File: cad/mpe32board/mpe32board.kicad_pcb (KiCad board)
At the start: 2 copper layers, 2 parts, among them J1 Conn_ST_STDC14, U2 STM32H743VIHx

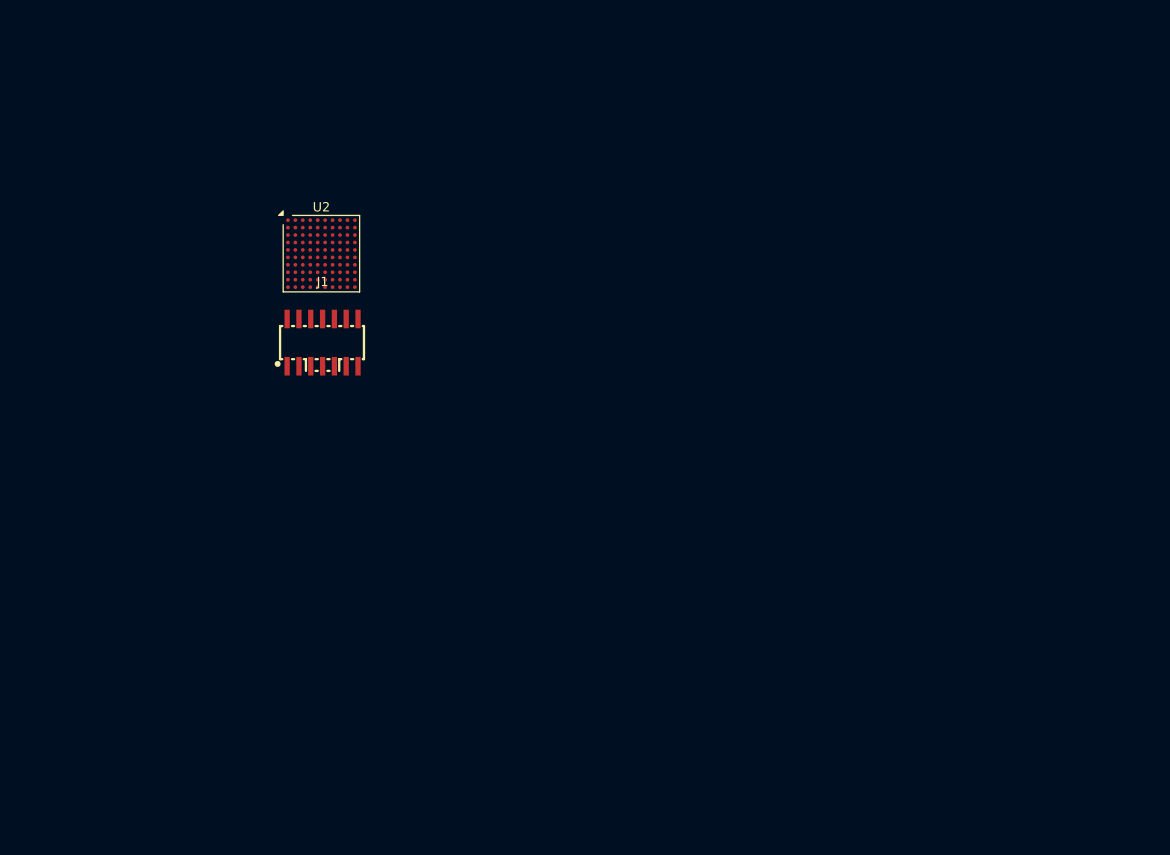
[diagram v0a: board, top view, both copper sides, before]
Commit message: pcb i2c mux + connectors
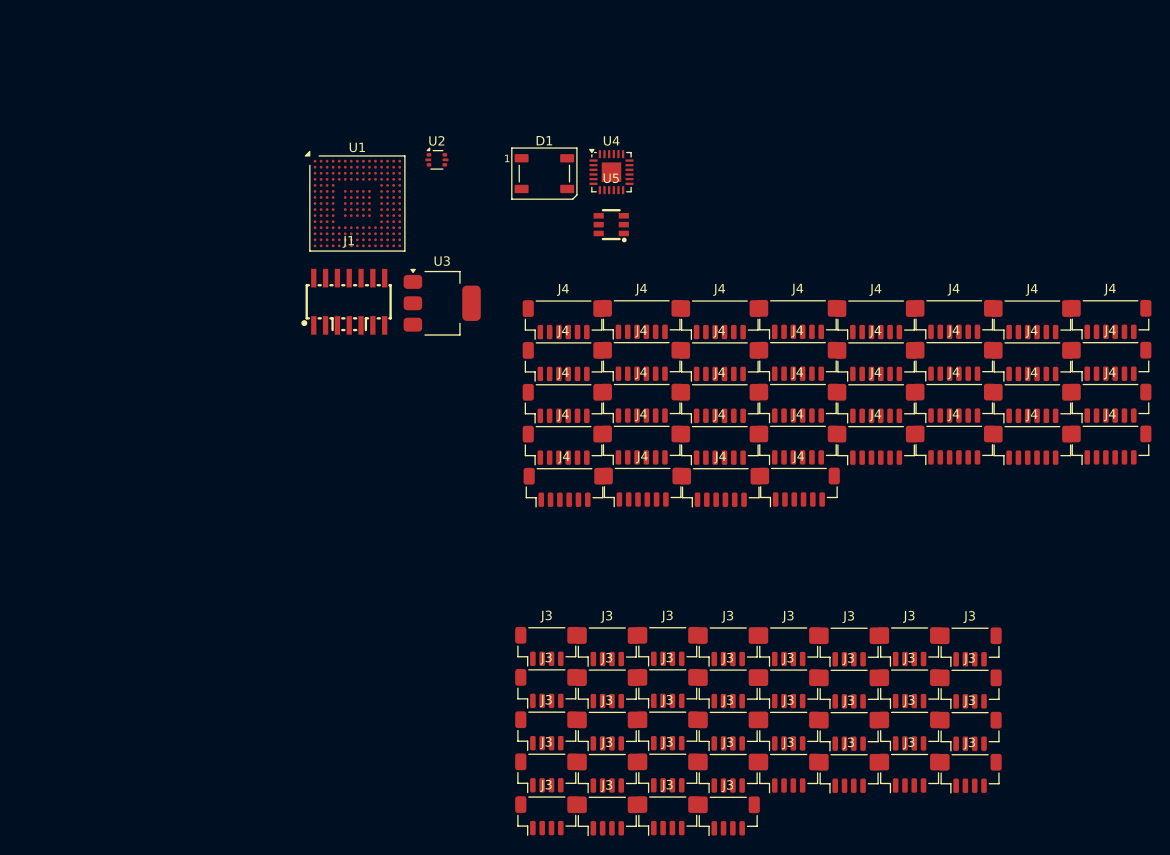
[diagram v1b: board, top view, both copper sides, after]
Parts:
- added D1: WS2812B, LED_SMD:LED_WS2812B_PLCC4_5.0x5.0mm_P3.2mm, F.Cu at (155.0, 84.3)
- added J3: Conn_01x04, Connector_JST:JST_SH_BM04B-SRSS-TB_1x04-1MP_P1.00mm_Vertical, F.Cu at (174.8, 153.3)
- added J3: Conn_01x04, Connector_JST:JST_SH_BM04B-SRSS-TB_1x04-1MP_P1.00mm_Vertical, F.Cu at (194.3, 139.7)
- added J3: Conn_01x04, Connector_JST:JST_SH_BM04B-SRSS-TB_1x04-1MP_P1.00mm_Vertical, F.Cu at (200.8, 139.7)
- added J3: Conn_01x04, Connector_JST:JST_SH_BM04B-SRSS-TB_1x04-1MP_P1.00mm_Vertical, F.Cu at (194.3, 144.2)
- added J3: Conn_01x04, Connector_JST:JST_SH_BM04B-SRSS-TB_1x04-1MP_P1.00mm_Vertical, F.Cu at (161.8, 139.7)
- added J3: Conn_01x04, Connector_JST:JST_SH_BM04B-SRSS-TB_1x04-1MP_P1.00mm_Vertical, F.Cu at (168.3, 144.2)
- added J3: Conn_01x04, Connector_JST:JST_SH_BM04B-SRSS-TB_1x04-1MP_P1.00mm_Vertical, F.Cu at (155.3, 135.1)
- added J3: Conn_01x04, Connector_JST:JST_SH_BM04B-SRSS-TB_1x04-1MP_P1.00mm_Vertical, F.Cu at (187.8, 148.8)
- added J3: Conn_01x04, Connector_JST:JST_SH_BM04B-SRSS-TB_1x04-1MP_P1.00mm_Vertical, F.Cu at (161.8, 148.8)
- added J3: Conn_01x04, Connector_JST:JST_SH_BM04B-SRSS-TB_1x04-1MP_P1.00mm_Vertical, F.Cu at (200.8, 135.2)
- added J3: Conn_01x04, Connector_JST:JST_SH_BM04B-SRSS-TB_1x04-1MP_P1.00mm_Vertical, F.Cu at (187.8, 144.2)
- added J3: Conn_01x04, Connector_JST:JST_SH_BM04B-SRSS-TB_1x04-1MP_P1.00mm_Vertical, F.Cu at (181.3, 139.7)
- added J3: Conn_01x04, Connector_JST:JST_SH_BM04B-SRSS-TB_1x04-1MP_P1.00mm_Vertical, F.Cu at (168.3, 148.7)
- added J3: Conn_01x04, Connector_JST:JST_SH_BM04B-SRSS-TB_1x04-1MP_P1.00mm_Vertical, F.Cu at (200.8, 148.8)
- added J3: Conn_01x04, Connector_JST:JST_SH_BM04B-SRSS-TB_1x04-1MP_P1.00mm_Vertical, F.Cu at (181.3, 148.8)
- added J3: Conn_01x04, Connector_JST:JST_SH_BM04B-SRSS-TB_1x04-1MP_P1.00mm_Vertical, F.Cu at (174.8, 144.2)
- added J3: Conn_01x04, Connector_JST:JST_SH_BM04B-SRSS-TB_1x04-1MP_P1.00mm_Vertical, F.Cu at (168.3, 139.7)
- added J3: Conn_01x04, Connector_JST:JST_SH_BM04B-SRSS-TB_1x04-1MP_P1.00mm_Vertical, F.Cu at (155.3, 139.7)
- added J3: Conn_01x04, Connector_JST:JST_SH_BM04B-SRSS-TB_1x04-1MP_P1.00mm_Vertical, F.Cu at (161.8, 144.2)
- added J3: Conn_01x04, Connector_JST:JST_SH_BM04B-SRSS-TB_1x04-1MP_P1.00mm_Vertical, F.Cu at (174.8, 135.2)
- added J3: Conn_01x04, Connector_JST:JST_SH_BM04B-SRSS-TB_1x04-1MP_P1.00mm_Vertical, F.Cu at (187.8, 135.2)
- added J3: Conn_01x04, Connector_JST:JST_SH_BM04B-SRSS-TB_1x04-1MP_P1.00mm_Vertical, F.Cu at (187.8, 139.7)
- added J3: Conn_01x04, Connector_JST:JST_SH_BM04B-SRSS-TB_1x04-1MP_P1.00mm_Vertical, F.Cu at (194.3, 148.8)
- added J3: Conn_01x04, Connector_JST:JST_SH_BM04B-SRSS-TB_1x04-1MP_P1.00mm_Vertical, F.Cu at (200.8, 144.2)
- added J3: Conn_01x04, Connector_JST:JST_SH_BM04B-SRSS-TB_1x04-1MP_P1.00mm_Vertical, F.Cu at (174.8, 148.8)
- added J3: Conn_01x04, Connector_JST:JST_SH_BM04B-SRSS-TB_1x04-1MP_P1.00mm_Vertical, F.Cu at (155.3, 153.3)
- added J3: Conn_01x04, Connector_JST:JST_SH_BM04B-SRSS-TB_1x04-1MP_P1.00mm_Vertical, F.Cu at (194.3, 135.2)
- added J3: Conn_01x04, Connector_JST:JST_SH_BM04B-SRSS-TB_1x04-1MP_P1.00mm_Vertical, F.Cu at (155.3, 144.2)
- added J3: Conn_01x04, Connector_JST:JST_SH_BM04B-SRSS-TB_1x04-1MP_P1.00mm_Vertical, F.Cu at (181.3, 144.2)
- added J3: Conn_01x04, Connector_JST:JST_SH_BM04B-SRSS-TB_1x04-1MP_P1.00mm_Vertical, F.Cu at (181.3, 135.2)
- added J3: Conn_01x04, Connector_JST:JST_SH_BM04B-SRSS-TB_1x04-1MP_P1.00mm_Vertical, F.Cu at (168.3, 135.1)
- added J3: Conn_01x04, Connector_JST:JST_SH_BM04B-SRSS-TB_1x04-1MP_P1.00mm_Vertical, F.Cu at (161.8, 135.2)
- added J3: Conn_01x04, Connector_JST:JST_SH_BM04B-SRSS-TB_1x04-1MP_P1.00mm_Vertical, F.Cu at (174.8, 139.7)
- added J3: Conn_01x04, Connector_JST:JST_SH_BM04B-SRSS-TB_1x04-1MP_P1.00mm_Vertical, F.Cu at (168.3, 153.3)
- added J3: Conn_01x04, Connector_JST:JST_SH_BM04B-SRSS-TB_1x04-1MP_P1.00mm_Vertical, F.Cu at (161.8, 153.3)
- added J3: Conn_01x04, Connector_JST:JST_SH_BM04B-SRSS-TB_1x04-1MP_P1.00mm_Vertical, F.Cu at (155.3, 148.7)
- added J4: Conn_01x06, Connector_JST:JST_SH_BM06B-SRSS-TB_1x06-1MP_P1.00mm_Vertical, F.Cu at (215.9, 100.0)
- added J4: Conn_01x06, Connector_JST:JST_SH_BM06B-SRSS-TB_1x06-1MP_P1.00mm_Vertical, F.Cu at (165.5, 104.5)
- added J4: Conn_01x06, Connector_JST:JST_SH_BM06B-SRSS-TB_1x06-1MP_P1.00mm_Vertical, F.Cu at (190.7, 100.0)
- added J4: Conn_01x06, Connector_JST:JST_SH_BM06B-SRSS-TB_1x06-1MP_P1.00mm_Vertical, F.Cu at (182.4, 118.0)
- added J4: Conn_01x06, Connector_JST:JST_SH_BM06B-SRSS-TB_1x06-1MP_P1.00mm_Vertical, F.Cu at (190.7, 109.0)
- added J4: Conn_01x06, Connector_JST:JST_SH_BM06B-SRSS-TB_1x06-1MP_P1.00mm_Vertical, F.Cu at (199.1, 109.0)
- added J4: Conn_01x06, Connector_JST:JST_SH_BM06B-SRSS-TB_1x06-1MP_P1.00mm_Vertical, F.Cu at (157.1, 100.0)
- added J4: Conn_01x06, Connector_JST:JST_SH_BM06B-SRSS-TB_1x06-1MP_P1.00mm_Vertical, F.Cu at (182.3, 104.5)
- added J4: Conn_01x06, Connector_JST:JST_SH_BM06B-SRSS-TB_1x06-1MP_P1.00mm_Vertical, F.Cu at (207.5, 109.0)
- added J4: Conn_01x06, Connector_JST:JST_SH_BM06B-SRSS-TB_1x06-1MP_P1.00mm_Vertical, F.Cu at (207.5, 113.5)
- added J4: Conn_01x06, Connector_JST:JST_SH_BM06B-SRSS-TB_1x06-1MP_P1.00mm_Vertical, F.Cu at (165.5, 109.0)
- added J4: Conn_01x06, Connector_JST:JST_SH_BM06B-SRSS-TB_1x06-1MP_P1.00mm_Vertical, F.Cu at (215.9, 104.5)
- added J4: Conn_01x06, Connector_JST:JST_SH_BM06B-SRSS-TB_1x06-1MP_P1.00mm_Vertical, F.Cu at (173.9, 113.5)
- added J4: Conn_01x06, Connector_JST:JST_SH_BM06B-SRSS-TB_1x06-1MP_P1.00mm_Vertical, F.Cu at (215.9, 113.5)
- added J4: Conn_01x06, Connector_JST:JST_SH_BM06B-SRSS-TB_1x06-1MP_P1.00mm_Vertical, F.Cu at (173.9, 104.5)
- added J4: Conn_01x06, Connector_JST:JST_SH_BM06B-SRSS-TB_1x06-1MP_P1.00mm_Vertical, F.Cu at (157.1, 104.5)
- added J4: Conn_01x06, Connector_JST:JST_SH_BM06B-SRSS-TB_1x06-1MP_P1.00mm_Vertical, F.Cu at (207.5, 100.0)
- added J4: Conn_01x06, Connector_JST:JST_SH_BM06B-SRSS-TB_1x06-1MP_P1.00mm_Vertical, F.Cu at (157.1, 113.5)
- added J4: Conn_01x06, Connector_JST:JST_SH_BM06B-SRSS-TB_1x06-1MP_P1.00mm_Vertical, F.Cu at (182.3, 109.0)
- added J4: Conn_01x06, Connector_JST:JST_SH_BM06B-SRSS-TB_1x06-1MP_P1.00mm_Vertical, F.Cu at (165.5, 113.5)
- added J4: Conn_01x06, Connector_JST:JST_SH_BM06B-SRSS-TB_1x06-1MP_P1.00mm_Vertical, F.Cu at (207.5, 104.5)
- added J4: Conn_01x06, Connector_JST:JST_SH_BM06B-SRSS-TB_1x06-1MP_P1.00mm_Vertical, F.Cu at (165.5, 100.0)
- added J4: Conn_01x06, Connector_JST:JST_SH_BM06B-SRSS-TB_1x06-1MP_P1.00mm_Vertical, F.Cu at (199.1, 104.5)
- added J4: Conn_01x06, Connector_JST:JST_SH_BM06B-SRSS-TB_1x06-1MP_P1.00mm_Vertical, F.Cu at (173.9, 100.0)
- added J4: Conn_01x06, Connector_JST:JST_SH_BM06B-SRSS-TB_1x06-1MP_P1.00mm_Vertical, F.Cu at (165.6, 118.0)
- added J4: Conn_01x06, Connector_JST:JST_SH_BM06B-SRSS-TB_1x06-1MP_P1.00mm_Vertical, F.Cu at (157.1, 109.0)
- added J4: Conn_01x06, Connector_JST:JST_SH_BM06B-SRSS-TB_1x06-1MP_P1.00mm_Vertical, F.Cu at (173.9, 109.0)
- added J4: Conn_01x06, Connector_JST:JST_SH_BM06B-SRSS-TB_1x06-1MP_P1.00mm_Vertical, F.Cu at (199.1, 100.0)
- added J4: Conn_01x06, Connector_JST:JST_SH_BM06B-SRSS-TB_1x06-1MP_P1.00mm_Vertical, F.Cu at (215.9, 109.0)
- added J4: Conn_01x06, Connector_JST:JST_SH_BM06B-SRSS-TB_1x06-1MP_P1.00mm_Vertical, F.Cu at (182.3, 100.0)
- added J4: Conn_01x06, Connector_JST:JST_SH_BM06B-SRSS-TB_1x06-1MP_P1.00mm_Vertical, F.Cu at (190.7, 104.5)
- added J4: Conn_01x06, Connector_JST:JST_SH_BM06B-SRSS-TB_1x06-1MP_P1.00mm_Vertical, F.Cu at (182.3, 113.5)
- added J4: Conn_01x06, Connector_JST:JST_SH_BM06B-SRSS-TB_1x06-1MP_P1.00mm_Vertical, F.Cu at (174.0, 118.0)
- added J4: Conn_01x06, Connector_JST:JST_SH_BM06B-SRSS-TB_1x06-1MP_P1.00mm_Vertical, F.Cu at (190.7, 113.5)
- added J4: Conn_01x06, Connector_JST:JST_SH_BM06B-SRSS-TB_1x06-1MP_P1.00mm_Vertical, F.Cu at (199.1, 113.5)
- added J4: Conn_01x06, Connector_JST:JST_SH_BM06B-SRSS-TB_1x06-1MP_P1.00mm_Vertical, F.Cu at (157.2, 118.0)
- added U1: STM32H743IIKx, Package_BGA:UFBGA-201_10x10mm_Layout15x15_P0.65mm, F.Cu at (134.9, 87.5)
- added U3: AMS1117-3.3, Package_TO_SOT_SMD:SOT-223-3_TabPin2, F.Cu at (144.1, 98.2)
- added U4: TCA9548ARGER, Package_DFN_QFN:Texas_RGE0024C_VQFN-24-1EP_4x4mm_P0.5mm_EP2.1x2.1mm, F.Cu at (162.2, 84.1)
- added U5: TMAG5273A1QDBVR, EasyEDA:SOT-23-6_L2.9-W1.6-P0.95-LS2.8-BR, F.Cu at (162.2, 89.8)
- U2: value STM32H743VIHx -> USBLC6-2P6; footprint Package_BGA:TFBGA-100_8x8mm_Layout10x10_P0.8mm -> Package_TO_SOT_SMD:SOT-666
- moved U2 16.0 mm to (143.5, 82.8)
- moved J1 5.24 mm to (134.1, 98.1)
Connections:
- J1 pad 10: unconnected-(J1-JTDI/NC-Pad10) -> JTDI
- J1 pad 12: unconnected-(J1-~{RST}-Pad12) -> NRST
- J1 pad 13: unconnected-(J1-VCP_RX-Pad13) -> LPUART1_RX
- J1 pad 14: unconnected-(J1-VCP_TX-Pad14) -> LPUART1_TX

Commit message: add sdram
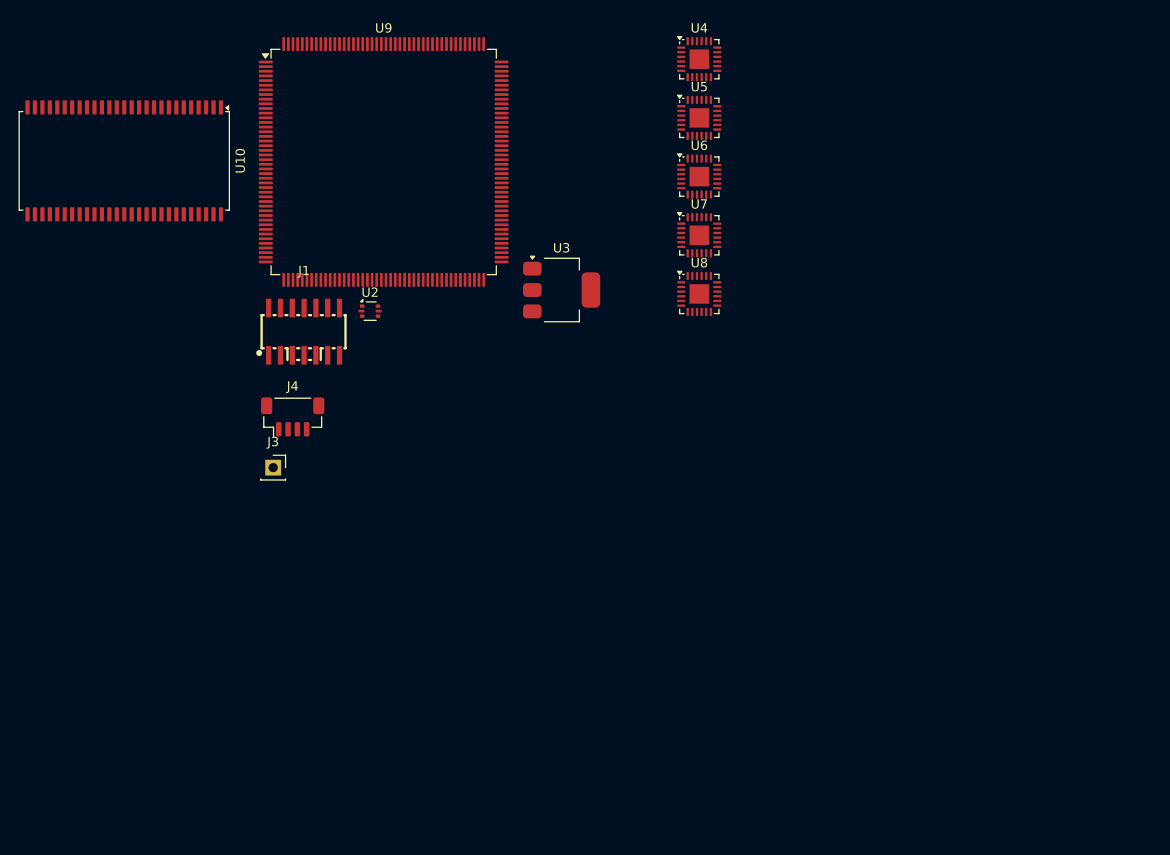
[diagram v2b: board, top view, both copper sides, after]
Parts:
- removed D1: WS2812B, LED_SMD:LED_WS2812B_PLCC4_5.0x5.0mm_P3.2mm
- removed the J3 at (174.8, 153.3)
- removed the J3 at (194.3, 139.7)
- removed the J3 at (200.8, 139.7)
- removed the J3 at (194.3, 144.2)
- removed the J3 at (161.8, 139.7)
- removed the J3 at (168.3, 144.2)
- removed the J3 at (155.3, 135.1)
- removed the J3 at (187.8, 148.8)
- removed the J3 at (161.8, 148.8)
- removed the J3 at (200.8, 135.2)
- removed the J3 at (187.8, 144.2)
- removed the J3 at (181.3, 139.7)
- removed the J3 at (168.3, 148.7)
- removed the J3 at (200.8, 148.8)
- removed the J3 at (181.3, 148.8)
- removed the J3 at (174.8, 144.2)
- removed the J3 at (168.3, 139.7)
- removed the J3 at (155.3, 139.7)
- removed the J3 at (161.8, 144.2)
- removed the J3 at (174.8, 135.2)
- removed the J3 at (187.8, 135.2)
- removed the J3 at (187.8, 139.7)
- removed the J3 at (194.3, 148.8)
- removed the J3 at (200.8, 144.2)
- removed the J3 at (174.8, 148.8)
- removed the J3 at (155.3, 153.3)
- removed the J3 at (194.3, 135.2)
- removed the J3 at (155.3, 144.2)
- removed the J3 at (181.3, 144.2)
- removed the J3 at (181.3, 135.2)
- removed the J3 at (168.3, 135.1)
- removed the J3 at (161.8, 135.2)
- removed the J3 at (174.8, 139.7)
- removed the J3 at (168.3, 153.3)
- removed the J3 at (161.8, 153.3)
- removed the J3 at (155.3, 148.7)
- removed the J4 at (215.9, 100.0)
- removed the J4 at (165.5, 104.5)
- removed the J4 at (190.7, 100.0)
- removed the J4 at (182.4, 118.0)
- removed the J4 at (190.7, 109.0)
- removed the J4 at (199.1, 109.0)
- removed the J4 at (157.1, 100.0)
- removed the J4 at (182.3, 104.5)
- removed the J4 at (207.5, 109.0)
- removed the J4 at (207.5, 113.5)
- removed the J4 at (165.5, 109.0)
- removed the J4 at (215.9, 104.5)
- removed the J4 at (173.9, 113.5)
- removed the J4 at (215.9, 113.5)
- removed the J4 at (173.9, 104.5)
- removed the J4 at (157.1, 104.5)
- removed the J4 at (207.5, 100.0)
- removed the J4 at (157.1, 113.5)
- removed the J4 at (182.3, 109.0)
- removed the J4 at (165.5, 113.5)
- removed the J4 at (207.5, 104.5)
- removed the J4 at (165.5, 100.0)
- removed the J4 at (199.1, 104.5)
- removed the J4 at (173.9, 100.0)
- removed the J4 at (165.6, 118.0)
- removed the J4 at (157.1, 109.0)
- removed the J4 at (173.9, 109.0)
- removed the J4 at (199.1, 100.0)
- removed the J4 at (215.9, 109.0)
- removed the J4 at (182.3, 100.0)
- removed the J4 at (190.7, 104.5)
- removed the J4 at (182.3, 113.5)
- removed the J4 at (174.0, 118.0)
- removed the J4 at (190.7, 113.5)
- removed the J4 at (199.1, 113.5)
- removed the J4 at (157.2, 118.0)
- removed U1: STM32H743IIKx, Package_BGA:UFBGA-201_10x10mm_Layout15x15_P0.65mm
- added J3: Conn_01x01_Socket, Connector_PinSocket_2.54mm:PinSocket_1x01_P2.54mm_Vertical, F.Cu at (125.9, 115.9)
- added J4: Conn_01x04, Connector_JST:JST_SH_BM04B-SRSS-TB_1x04-1MP_P1.00mm_Vertical, F.Cu at (128.0, 110.5)
- added U10: W9812G6KH-75, Package_SO:TSOP-II-54_22.2x10.16mm_P0.8mm, F.Cu at (109.9, 82.9)
- added U6: TCA9548ARGER, Package_DFN_QFN:Texas_RGE0024C_VQFN-24-1EP_4x4mm_P0.5mm_EP2.1x2.1mm, F.Cu at (171.7, 84.6)
- added U7: TCA9548ARGER, Package_DFN_QFN:Texas_RGE0024C_VQFN-24-1EP_4x4mm_P0.5mm_EP2.1x2.1mm, F.Cu at (171.7, 90.9)
- added U8: TCA9548ARGER, Package_DFN_QFN:Texas_RGE0024C_VQFN-24-1EP_4x4mm_P0.5mm_EP2.1x2.1mm, F.Cu at (171.7, 97.2)
- added U9: STM32H743IITx, Package_QFP:LQFP-176_24x24mm_P0.5mm, F.Cu at (137.8, 83.0)
- U5: value TMAG5273A1QDBVR -> TCA9548ARGER; footprint EasyEDA:SOT-23-6_L2.9-W1.6-P0.95-LS2.8-BR -> Package_DFN_QFN:Texas_RGE0024C_VQFN-24-1EP_4x4mm_P0.5mm_EP2.1x2.1mm
- moved U2 17.8 mm to (136.3, 99.1)
- moved U4 15.4 mm to (171.7, 72.0)
- moved U5 14.9 mm to (171.7, 78.3)
- moved U3 12.9 mm to (156.9, 96.8)
- moved J1 5.82 mm to (129.2, 101.3)
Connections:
- U4 pad 1: SD0 -> 0_SD0
- U4 pad 10: unconnected-(U4-SD4-Pad10) -> 4_SD4
- U4 pad 11: unconnected-(U4-SC4-Pad11) -> 4_SC4
- U4 pad 12: unconnected-(U4-SD5-Pad12) -> 5_SD5
- U4 pad 13: unconnected-(U4-SC5-Pad13) -> 5_SC5
- U4 pad 14: unconnected-(U4-SD6-Pad14) -> 6_SD6
- U4 pad 15: unconnected-(U4-SC6-Pad15) -> 6_SC6
- U4 pad 16: unconnected-(U4-SD7-Pad16) -> 7_SD7
- U4 pad 17: unconnected-(U4-SC7-Pad17) -> 7_SC7
- U4 pad 18: unconnected-(U4-A2-Pad18) -> GND
- U4 pad 19: unconnected-(U4-SCL-Pad19) -> SCL_0
- U4 pad 2: SC0 -> 0_SC0
- U4 pad 20: unconnected-(U4-SDA-Pad20) -> SDA_0
- U4 pad 22: unconnected-(U4-A0-Pad22) -> GND
- U4 pad 23: unconnected-(U4-A1-Pad23) -> GND
- U4 pad 24: unconnected-(U4-~{RESET}-Pad24) -> RESET_0
- U4 pad 3: unconnected-(U4-SD1-Pad3) -> 1_SD1
- U4 pad 4: unconnected-(U4-SC1-Pad4) -> 1_SC1
- U4 pad 5: unconnected-(U4-SD2-Pad5) -> 2_SD2
- U4 pad 6: unconnected-(U4-SC2-Pad6) -> 2_SC2
- U4 pad 7: unconnected-(U4-SD3-Pad7) -> 3_SD3
- U4 pad 8: unconnected-(U4-SC3-Pad8) -> 3_SC3
- U5 pad 1: unconnected-(U5-SCL-Pad1) -> 8_SD0
- U5 pad 2: unconnected-(U5-GND-Pad2) -> 8_SC0
- U5 pad 3: unconnected-(U5-GND(TEST)-Pad3) -> 9_SD1
- U5 pad 4: unconnected-(U5-VCC-Pad4) -> 9_SC1
- U5 pad 5: unconnected-(U5-~{INT}-Pad5) -> 10_SD2
- U5 pad 6: unconnected-(U5-SDA-Pad6) -> 10_SC2
